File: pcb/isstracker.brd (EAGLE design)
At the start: 68.6 x 54.3 mm, 23 parts, among them IC1 74LS125N, J1 MOTOR_RIGHT, J2 CONTROL, J3 MOTOR_LEFT, J4 DISPLAY, J5 DEC_POSITION, J7 LED, J8 UART, J9 DISTANCE, U1 ARGON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

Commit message: Fixing PCB to use the new IR sensor instead.
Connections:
- net +3V3: now also J9.1; no longer J9.2
- net DISTANCE: now also J9.2; no longer J9.1
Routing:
- net +3V3: track 25.5 -> 21.5 mm
- net DISTANCE: track 12.0 -> 11.0 mm
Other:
- board text added: "5 Volt On"
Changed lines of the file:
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@@
 <text x="38.608" y="44.069" size="0.8128" layer="121">Lumenati</text>
 <text x="3.429" y="0.127" size="0.8128" layer="121">B</text>
+<text x="16.764" y="49.53" size="1.016" layer="121" rot="R90">5 Volt
+On</text>
 </plain>
 <attributes>
@@
 </element>
 <element name="J8" library="SparkFun-Connectors" library_urn="urn:adsk.eagle:library:513" package="1X03" package3d_urn="urn:adsk.eagle:package:38063/1" value="UART" x="8.89" y="2.54" smashed="yes" rot="R180"/>
-<element name="LED3" library="adafruit" library_urn="urn:adsk.eagle:library:420" package="LED3MM" package3d_urn="urn:adsk.eagle:package:6240537/1" value="BLUE" x="19.05" y="50.8" smashed="yes" rot="R270">
-<attribute name="VALUE" x="10.795" y="49.149" size="1.27" layer="27" ratio="10"/>
-</element>
+<element name="LED3" library="adafruit" library_urn="urn:adsk.eagle:library:420" package="LED3MM" package3d_urn="urn:adsk.eagle:package:6240537/1" value="BLUE" x="19.05" y="50.8" smashed="yes" rot="R270"/>
 <element name="U1" library="Particle-Devices" package="ARGON" package3d_urn="urn:adsk.eagle:package:10606117/2" value="ARGON" x="12.7" y="-3.81" smashed="yes">
 <attribute name="NAME" x="12.7" y="-5.08" size="1.27" layer="21" align="top-left"/>
@@
 <contactref element="U1" pad="2"/>
 <contactref element="J5" pad="1"/>
-<wire x1="10.16" y1="41.91" x2="5.08" y2="41.91" width="0.8128" layer="16"/>
-<wire x1="10.16" y1="41.91" x2="13.97" y2="38.1" width="0.8128" layer="16"/>
-<contactref element="J9" pad="2"/>
-<wire x1="5.08" y1="41.91" x2="3.81" y2="41.91" width="0.8128" layer="16"/>
-<wire x1="3.81" y1="41.91" x2="2.54" y2="40.64" width="0.8128" layer="16"/>
-<wire x1="2.54" y1="31.75" x2="3.81" y2="30.48" width="0.8128" layer="16"/>
-<wire x1="3.81" y1="30.48" x2="5.08" y2="30.48" width="0.8128" layer="16"/>
-<wire x1="2.54" y1="40.64" x2="2.54" y2="31.75" width="0.8128" layer="16"/>
+<contactref element="J9" pad="1"/>
+<wire x1="13.97" y1="38.1" x2="8.89" y2="33.02" width="1.27" layer="16"/>
+<wire x1="8.89" y1="33.02" x2="5.08" y2="33.02" width="1.27" layer="16"/>
+<wire x1="5.08" y1="41.91" x2="10.16" y2="41.91" width="1.27" layer="16"/>
+<wire x1="10.16" y1="41.91" x2="13.97" y2="38.1" width="1.27" layer="16"/>
 </signal>
 <signal name="MTR_EN">
@@
 </signal>
 <signal name="DISTANCE">
-<contactref element="J9" pad="1"/>
 <contactref element="U1" pad="7"/>
-<wire x1="5.08" y1="33.02" x2="12.7" y2="25.4" width="0.4064" layer="1"/>
-<wire x1="12.7" y1="25.4" x2="13.97" y2="25.4" width="0.4064" layer="1"/>
+<contactref element="J9" pad="2"/>
+<wire x1="5.08" y1="30.48" x2="8.89" y2="30.48" width="0.4064" layer="1"/>
+<wire x1="8.89" y1="30.48" x2="13.97" y2="25.4" width="0.4064" layer="1"/>
 </signal>
 <signal name="RST">

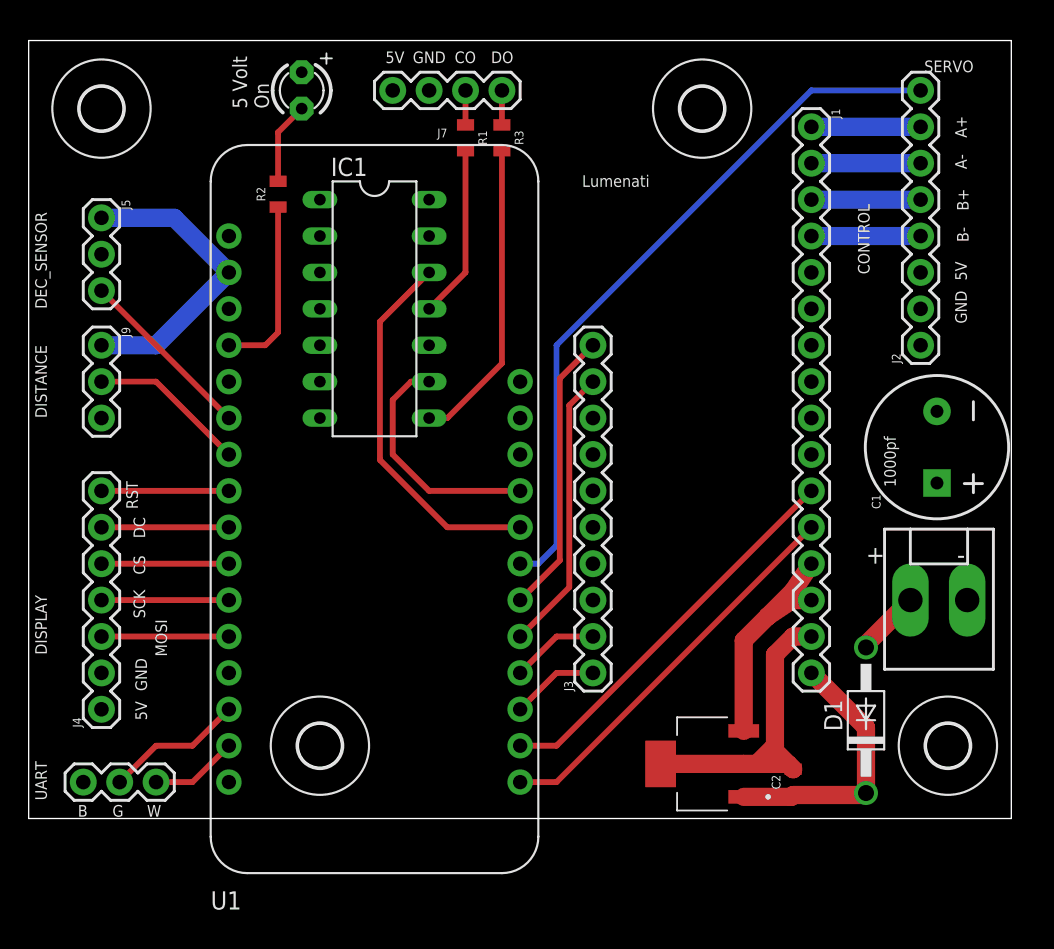
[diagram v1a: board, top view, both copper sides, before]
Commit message: Version 47:
* Only wake motor from sleep IFF we are going to move the motor
* Clean up some extra logging
* Add LED controls for the globe lighting
* This includes the first PCB sent out for production at OSHPark
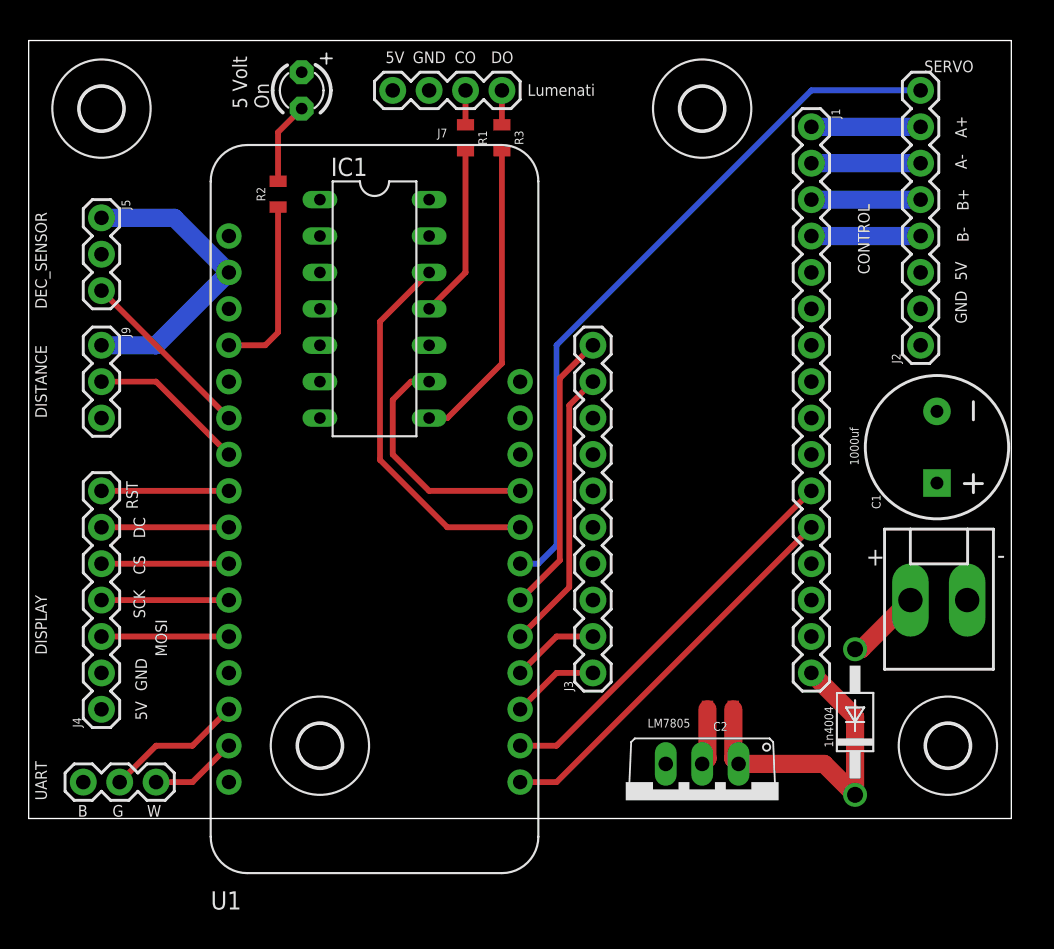
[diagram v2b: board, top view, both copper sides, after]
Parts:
- removed VR1: LM7805MP/NOPB, LM7805MP_NOPB:VREG_LM7805MP/NOPB
- added IC2: 7805TV, linear:TO220V
- moved C2 7.18 mm to (48.3, 7.62), turned to 180 degrees
- moved D1 0.77 mm to (57.7, 6.73)
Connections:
- net +12V: now also IC2.1; no longer VR1.1
- net +5V: now also IC2.3; no longer VR1.3
- net GND: now also IC2.2; no longer VR1.2, VR1.4
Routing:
- net GND: track 35.3 -> 16.5 mm
- net +5V: track 16.9 -> 0.00 mm
- net +12V: track 18.6 -> 22.8 mm
- net N$1: track 4.59 -> 5.28 mm
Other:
- board text added: "1000uf"
- board text added: "1n4004"
- board text added: "LM7805"
- board text removed: "1000pf"

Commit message: Updating to the latest PCB to fix breaking issues
* Fixed capacitor sets for both boards to be larger and polarized on the
LDO's
* Fixed left track for motor board as it was 1 pin too short
* Switched from Declination to Azimuth
* Moved Azimuth signaling to the internal board to allow for movement
* Removed resistors on 5V LED signal buffer
* Switch LED pinout to match the Lumenati ordering
* Internal board got a polarized capacitor
* Internal board layout moved around to better match reality
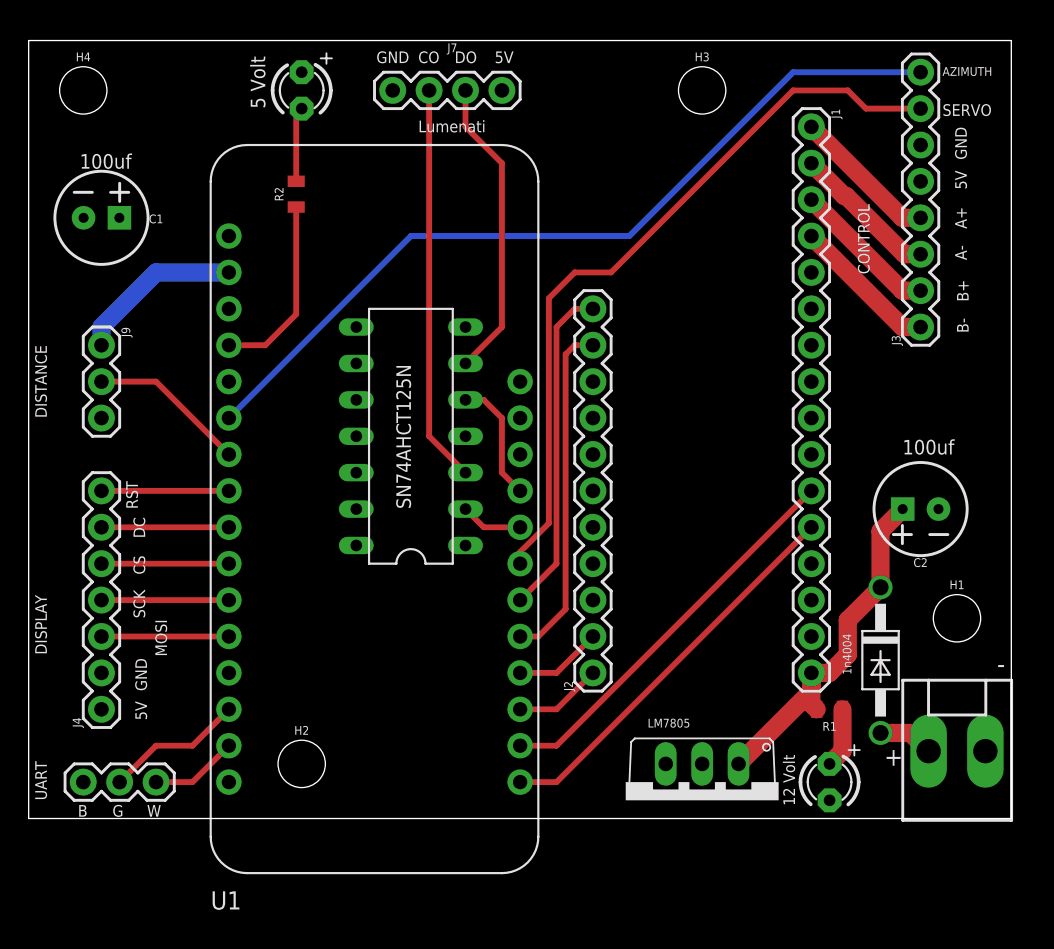
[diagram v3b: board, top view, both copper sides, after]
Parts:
- removed J5: DEC_POSITION, SparkFun-Connectors:1X03
- removed R3: 300, SparkFun-Resistors:0805
- added LED1: RED, adafruit:LED3MM
- C1: value 1000uf -> 100uF; device SparkFun-Capacitors:CPOL-RADIAL-5MM-10MM -> SparkFun-Capacitors:CPOL-RADIAL-2.5MM-6.5MM
- C2: value 10uf -> 100uF; device SparkFun-Capacitors:0805 -> SparkFun-Capacitors:CPOL-RADIAL-2.5MM-6.5MM
- H1, H2, H3, H4: value MOUNT-HOLE3.0 -> STAND-OFF; device holes:3,0 -> SparkFun-Hardware:STAND-OFF
- IC1: value 74LS125N -> SN74AHCT125N
- IC2: value 7805TV -> L7805CV
- J2: value CONTROL -> MOTOR_LEFT; device SparkFun-Connectors:1X08 -> SparkFun-Connectors:1X11
- J3: value MOTOR_LEFT -> CONTROL; device SparkFun-Connectors:1X10 -> SparkFun-Connectors:1X08
- R1: value 300 -> 1k
- moved C1 60.4 mm to (5.08, 41.9), turned to 0 degrees
- moved R1 47.3 mm to (55.9, 7.62), turned to 180 degrees
- moved H1 45.3 mm to (64.8, 14.0)
- moved H2 45.1 mm to (19.1, 3.81)
- moved J3 33.2 mm to (62.2, 34.3)
- moved J2 32.3 mm to (39.4, 10.2)
- moved C2 19.8 mm to (62.2, 21.6)
- moved X1 10.6 mm to (64.8, 4.70)
- moved IC1 9.25 mm to (26.7, 26.7), turned to 90 degrees
- moved J7 7.62 mm to (25.4, 50.8), turned to 0 degrees
- moved D1 4.67 mm to (59.4, 11.0), turned to 270 degrees
- moved H4 1.80 mm to (3.81, 50.8)
- moved R2 1.27 mm to (18.7, 43.6)
- moved H3 1.27 mm to (47.0, 50.8)
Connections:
- removed net DEC: J5.3, U1.6
- removed net N$3: J7.1, R3.1
- new net AZIMUTH: J3.8, U1.6
- net +12V: now also R1.2
- net +3V3: no longer J5.1
- net +5V: now also C1.1, J3.5; no longer C1.+, J1.13, J1.14, J2.3
- net A+: now also J3.4; no longer J2.7
- net A-: now also J3.3; no longer J2.6
- net B+: now also J3.2; no longer J2.5
- net B-: now also J3.1; no longer J2.4
- net CO: now also IC1.3, J7.2; no longer IC1.11, R1.2
- net DO: now also IC1.6, J7.3; no longer IC1.8, R3.2
- net GND: now also C1.2, IC1.11, IC1.8, J2.3, J3.6, J7.1, LED1.K; no longer C1.-, IC1.3, IC1.6, J2.2, J3.3, J5.2, J7.3
- net LED_CO: now also IC1.2; no longer IC1.12
- net LED_DO: now also IC1.5; no longer IC1.9
- net MTR_DIR: now also J2.1; no longer J3.1
- net MTR_MS1: now also J2.10; no longer J3.9
- net MTR_SLP: now also J2.11; no longer J3.10
- net MTR_STEP: now also J2.2; no longer J3.2
- net N$2: now also LED1.A; no longer J7.2
- net SERVO: now also J3.7; no longer J2.8
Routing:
- net AZIMUTH: track 0.00 -> 58.3 mm
- net LED_CO: track 26.2 -> 4.34 mm
- net CO: track 12.1 -> 27.7 mm
- net DEC: track 12.6 -> 0.00 mm
- net +3V3: track 21.5 -> 11.7 mm
- net LED_DO: track 16.8 -> 8.67 mm
- net MTR_MS1: track 19.9 -> 23.9 mm
- net GND: track 16.5 -> 13.1 mm
- net MTR_SLP: track 19.9 -> 23.2 mm
- net +12V: track 22.8 -> 26.0 mm
- net A-: track 7.62 -> 10.3 mm
- net B-: track 7.62 -> 10.3 mm
- net B+: track 7.62 -> 10.3 mm
- net A+: track 7.62 -> 10.3 mm
- net N$3: track 2.40 -> 0.00 mm
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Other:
- board text added: "100uf"
- board text added: "12 Volt"
- board text added: "5 Volt"
- board text added: "AZIMUTH"
- board text added: "ISS Position Tracker (C) Peter Buelow February, 2021 Version 1.1"
- board text added: "SN74AHCT125N"
- board text removed: "1000uf"
- board text removed: "5 Volt On"
- board text removed: "DEC_SENSOR"
- board text removed: "ISS Position Tracker (C) Peter Buelow January, 2021 Version 1.0"

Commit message: Adding laser control
* Hookup an NPN to be able to turn the laser on/off via A0
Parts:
- removed J3: CONTROL, SparkFun-Connectors:1X08
- added J5: CONTROL, SparkFun-Connectors:1X09
- moved H3 1.02 mm to (46.0, 50.8)
- moved D1 0.65 mm to (58.8, 11.2)
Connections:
- new net LASER: J5.9, U1.5
- net +5V: now also J5.5; no longer J3.5
- net A+: now also J5.4; no longer J3.4
- net A-: now also J5.3; no longer J3.3
- net AZIMUTH: now also J5.8; no longer J3.8
- net B+: now also J5.2; no longer J3.2
- net B-: now also J5.1; no longer J3.1
- net GND: now also J5.6; no longer J3.6
- net SERVO: now also J5.7; no longer J3.7
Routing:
- net LASER: track 0.00 -> 58.5 mm
- net B-: track 10.3 -> 14.1 mm
- net B+: track 10.3 -> 14.1 mm
- net A-: track 10.3 -> 14.1 mm
- net A+: track 10.3 -> 13.3 mm
- net SERVO: track 51.8 -> 53.2 mm
- net AZIMUTH: track 58.3 -> 59.0 mm
- net N$1: track 3.88 -> 4.57 mm
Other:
- board text added: "ISS Position Tracker (C) Peter Buelow February, 2021 Version 1.2"
- board text added: "LASER"
- board text removed: "ISS Position Tracker (C) Peter Buelow February, 2021 Version 1.1"

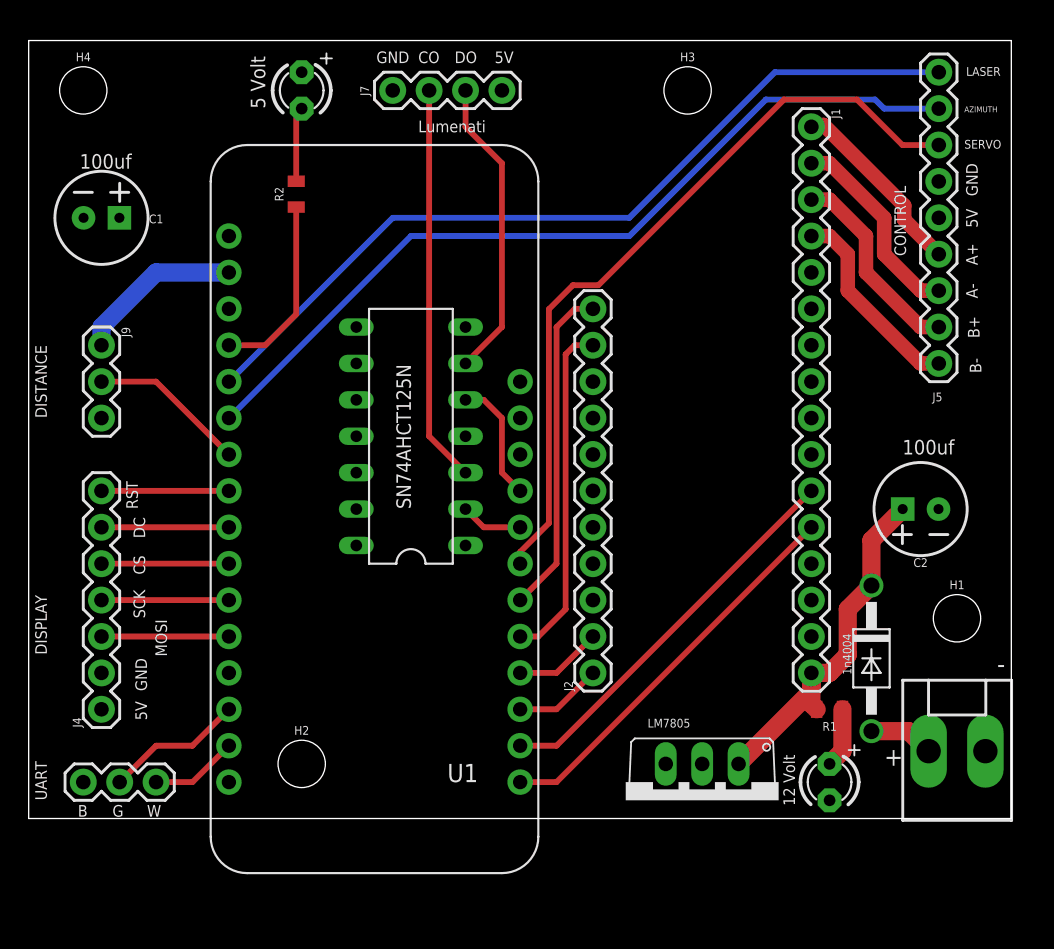
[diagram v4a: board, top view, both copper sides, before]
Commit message: Lots of changes
* Dropped LED's and LASER control
* Renamed DECLINATION to AZIMUTH
* Moved AZIMUTH control hookup into the globe (it needs to spin freely)

I couldn't make the LED's fit and shine without casting shadows inside
the globe. Plus, there wasn't much room, and it required more wires to
make work. No a critical problem, but the challenges outweighed the
benefits. I'm going to water color paint the globe now.

I also removed the LASER control, the manufacturer said don't duty cycle
it, the built in controls take care of it. This isn't supposed to be on
constantly anyway.
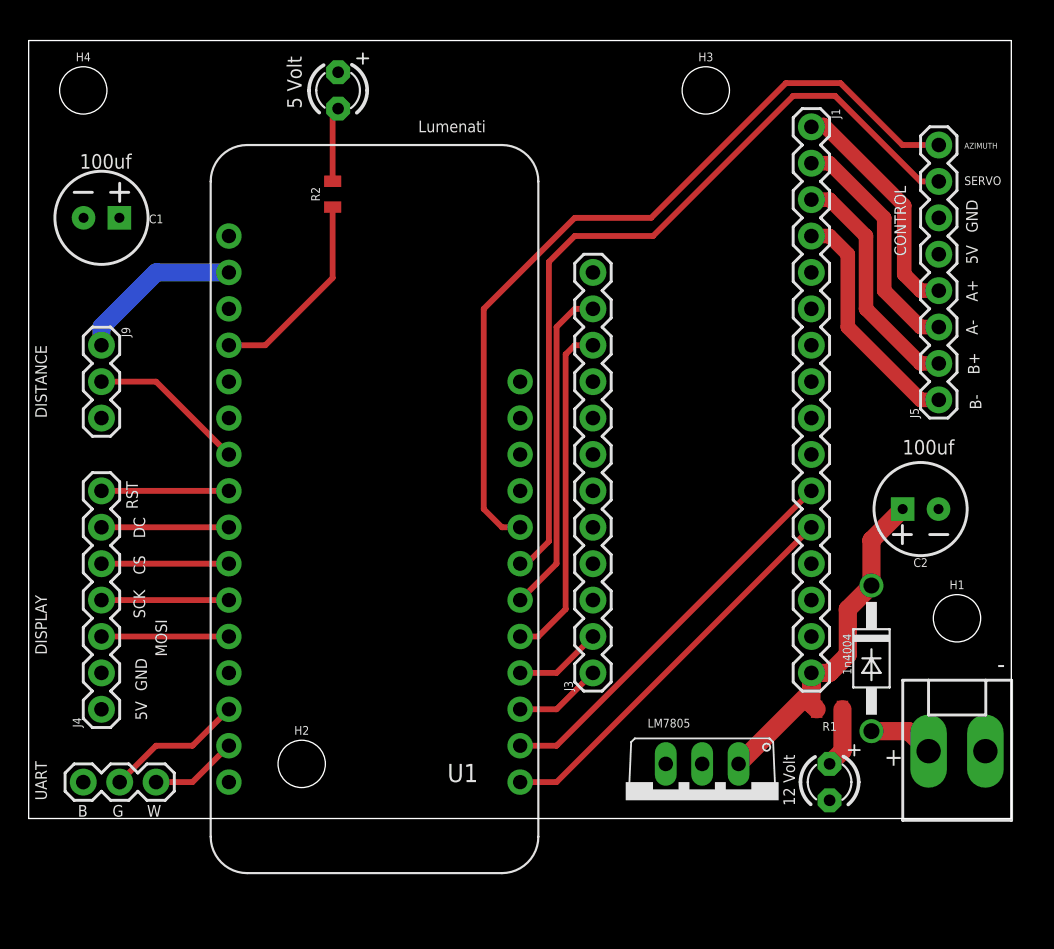
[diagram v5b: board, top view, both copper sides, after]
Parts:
- removed IC1: SN74AHCT125N, adafruit:DIL14
- removed J2: MOTOR_LEFT, SparkFun-Connectors:1X11
- removed J7: LED, SparkFun-Connectors:1X04
- added J3: MOTOR_LEFT, SparkFun-Connectors:1X12
- J5: device SparkFun-Connectors:1X09 -> SparkFun-Connectors:1X08
- moved J5 2.54 mm to (63.5, 29.2)
- moved LED3 2.54 mm to (21.6, 50.8)
- moved R2 2.54 mm to (21.2, 43.6)
- moved H3 1.27 mm to (47.2, 50.8)
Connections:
- removed net CO: IC1.3, J7.2
- removed net DO: IC1.6, J7.3
- removed net LASER: J5.9, U1.5
- removed net LED_CO: IC1.2, U1.24
- removed net LED_DO: IC1.5, U1.25
- net +5V: no longer IC1.14, J7.4
- net AZIMUTH: now also U1.24; no longer U1.6
- net GND: now also J3.3; no longer IC1.1, IC1.10, IC1.11, IC1.13, IC1.4, IC1.7, IC1.8, J2.3, J7.1
- net MTR_DIR: now also J3.1; no longer J2.1
- net MTR_MS1: now also J3.10; no longer J2.10
- net MTR_SLP: now also J3.11; no longer J2.11
- net MTR_STEP: now also J3.2; no longer J2.2
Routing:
- net LASER: track 58.5 -> 0.00 mm
- net CO: track 27.7 -> 0.00 mm
- net DO: track 21.2 -> 0.00 mm
- net LED_DO: track 8.67 -> 0.00 mm
- net LED_CO: track 4.34 -> 0.00 mm
- net SERVO: track 53.2 -> 56.6 mm
- net A+: track 13.3 -> 16.5 mm
- net B-: track 14.1 -> 16.6 mm
- net B+: track 14.1 -> 16.6 mm
- net A-: track 14.1 -> 16.6 mm
- net AZIMUTH: track 59.0 -> 57.1 mm
- net GND: track 13.1 -> 14.1 mm
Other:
- board text added: "ISS Position Tracker (C) Peter Buelow February, 2021 Version 1.3"
- board text removed: "CO"
- board text removed: "DO"
- board text removed: "ISS Position Tracker (C) Peter Buelow February, 2021 Version 1.2"
- board text removed: "LASER"
- board text removed: "SN74AHCT125N"
